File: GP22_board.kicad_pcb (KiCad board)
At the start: 2 copper layers, 100 x 100 mm, 115 parts, among them CON1 5V power input, IC1 ATMEGA328P-A, P1 TTLOut1, P10 CONN_02X02, P11 CONN_02X02, P12 CONN_02X02, P13 TTLOut2, P14 TTLOut3, P15 CONN_01X03, P2 SineInput, P3 TTLInput, P4 USB_OTG, P5 ICSP, P6 StraightThroughInput, P7 CONN_02X02, P8 CONN_02X02, P9 CONN_02X02, SW1 ROTARY_SWITCH_ALPS_SRBM, SW2 ROTARY_SWITCH_ALPS_SRBM, SW3 ROTARY_SWITCH_ALPS_SRBM, U1 RS 252-210, U10 XC6206, U11 ISO7242, U12 FT232RL, U2 GP22, U3 LTC6957-4, U4 ISO3088, U5 IDT49FCT, U6 LD1117S33TR, U7 MC74VHC1GT04, U8 SN74LV8154, U9 SC74HC165N, X1 TSX-3225 X1E0000210013, Y1 4MHz, Y2 32.768 kHz

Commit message: Board nearly done
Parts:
- added D6: ESDA5V3SC6, TO_SOT_Packages_SMD:SOT-23-5_HandSoldering, F.Cu at (190.5, 47.2)
- added D7: ESDA5V3SC6, TO_SOT_Packages_SMD:SOT-23-5_HandSoldering, F.Cu at (173.3, 52.5)
- moved C17 285.0 mm to (193.6, 81.2)
- moved R34 253.7 mm to (192.2, 84.6), turned to 90 degrees
- moved R33 225.6 mm to (187.8, 90.4), turned to 270 degrees
- moved C15 216.9 mm to (191.6, 100.4), turned to 270 degrees
- moved C16 195.2 mm to (186.6, 93.8), turned to 180 degrees
- moved Y1 169.8 mm to (205.0, 96.2), turned to 180 degrees
- moved Y2 138.6 mm to (210.3, 84.5), turned to 180 degrees
- moved C22 137.6 mm to (200.6, 102.8), turned to 180 degrees
- moved R36 133.2 mm to (200.6, 100.4), turned to 180 degrees
- moved C21 131.8 mm to (211.6, 96.4), turned to 270 degrees
- moved C23 130.7 mm to (214.0, 96.6), turned to 90 degrees
- moved R35 129.3 mm to (209.2, 96.4), turned to 270 degrees
- moved R37 120.6 mm to (212.2, 100.2), turned to 180 degrees
- moved U10 120.6 mm to (206.6, 101.0), turned to 180 degrees
- moved U8 93.7 mm to (231.0, 76.4)
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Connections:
- D1 pad 1: /InputCoupling/OutputS- -> (no net)
- D1 pad 3: /InputCoupling2/OutputS+ -> /InputCoupling/InputSignal
- D1 pad 4: /StraightThrough -> /InputCoupling/InputGnd
- D1 pad 5: /InputCoupling/OutputS+ -> (no net)
- SW1 pad 1b: /StraightThrough -> /TTLBuffered
- SW1 pad 2b: /SineRectified -> /StraightThrough
- SW1 pad 4a: /TTLBuffered -> /SineRectified
- SW2 pad 1b: /StraightThrough -> /TTLBuffered
- SW2 pad 2b: /SineRectified -> /StraightThrough
- SW2 pad 4a: /TTLBuffered -> /SineRectified
- SW3 pad 1b: /StraightThrough -> /TTLBuffered
- SW3 pad 2b: /SineRectified -> /StraightThrough
- SW3 pad 4a: /TTLBuffered -> /SineRectified
- U5 pad 2: /TTLBufferedOut2 -> /TTLBufferedOut3
- U5 pad 3: /TTLBufferedOut1 -> /TTLBufferedOut2
- U5 pad 4: /TTLBufferedOut3 -> /TTLBufferedOut1
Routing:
- net /TTLBufferedOut1: track 0.00 -> 84.7 mm
- net /TTLBufferedOut3: track 0.00 -> 83.8 mm
- net /TTLBufferedOut2: track 0.00 -> 81.8 mm
- net Net-(U8-Pad15): track 0.00 -> 38.0 mm
- net Net-(U8-Pad14): track 0.00 -> 36.7 mm
- net Net-(U8-Pad13): track 0.00 -> 35.5 mm
- net Net-(U8-Pad12): track 0.00 -> 34.2 mm
- net /GP22_VIO: track 0.00 -> 29.8 mm
- net /StraightThrough: track 168.1 -> 139.2 mm
- net /InputCoupling2/OutputS+: track 32.2 -> 60.4 mm
- net /InputCoupling2/InputSignal: track 9.79 -> 34.7 mm
- net /InputCoupling2/InputGnd: track 10.9 -> 35.1 mm
- net /SineRectified: track 103.0 -> 84.8 mm
- net /GP22_START: track 62.2 -> 46.5 mm
- net /TTLBufferedOut_toCounter: track 0.00 -> 12.9 mm
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- added copper zone on In2.Cu, net +3V3
- added copper zone on In2.Cu, net /GP22_VCC
- added copper zone on In1.Cu, net GND
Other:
- copper layers 2 -> 4

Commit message: DRC passes
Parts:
- removed C20: 100n, Capacitors_SMD:C_0805_HandSoldering
- removed R24, R25, R30, R31: 10k, Resistors_SMD:R_0805_HandSoldering
- added C26: 100n, Capacitors_SMD:C_0805_HandSoldering, F.Cu at (202.3, 89.5)
- added C27: 100n, Capacitors_SMD:C_0805_HandSoldering, F.Cu at (213.2, 87.1)
- added P16: FILT_SEL, Pin_Headers:Pin_Header_Straight_2x02_Pitch2.54mm, F.Cu at (217.2, 60.0)
- P15: value CONN_01X03 -> PWR_SEL
- moved C2 203.3 mm to (200.7, 99.9), turned to 180 degrees
- moved C1 197.4 mm to (201.4, 92.5)
- moved R2 194.4 mm to (199.1, 108.8), turned to 180 degrees
- moved R5 190.6 mm to (195.1, 99.1), turned to 270 degrees
- moved R9 183.3 mm to (210.3, 62.0)
- moved R6 179.0 mm to (210.0, 81.2)
- moved C3 174.1 mm to (210.0, 79.3), turned to 180 degrees
- moved R1 173.8 mm to (201.8, 84.4)
- moved R7 171.2 mm to (210.3, 60.0), turned to 180 degrees
- moved C5 164.2 mm to (206.3, 81.8), turned to 90 degrees
- moved R4 163.8 mm to (201.8, 82.5)
- moved CON1 160.2 mm to (220.8, 48.0), turned to 180 degrees
- moved C18 156.6 mm to (239.7, 59.6)
- moved U6 156.3 mm to (232.9, 62.8), turned to 180 degrees
- moved C19 138.1 mm to (240.7, 65.7)
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- renumbered C2 to C1, C1 to C2
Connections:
- net Net-(C12-Pad2) renamed /G1
- net Net-(C13-Pad2) renamed /G2
- net Net-(C14-Pad2) renamed /G3
- C1 pad 2: Net-(C2-Pad2) -> Net-(C1-Pad2)
- C2 pad 2: Net-(C1-Pad2) -> Net-(C2-Pad2)
- CON1 pad 1: Net-(C18-Pad1) -> Net-(CON1-Pad1)
- IC1 pad 11: /~CTR_CLR -> /REG_DATA
- IC1 pad 12: /CTR_LOAD -> /CTR_BIT_SEL
- IC1 pad 13: /CTR_BIT_SEL -> /CTR_LOAD
- IC1 pad 23: /LTC_FILTB -> /GP22_INT
- IC1 pad 24: /LTC_FILTA -> /GP22_EN_START
- IC1 pad 25: /GP22_INT -> /GP22_EN_STOP1
- IC1 pad 26: /GP22_EN_START -> /GP22_EN_STOP2
- IC1 pad 27: /GP22_EN_STOP1 -> /~CTR_CLR
- IC1 pad 28: /GP22_EN_STOP2 -> /REG_CLK
- IC1 pad 30: /REG_DATA -> /DIYino/D0/RX
- IC1 pad 31: /REG_LOAD -> /DIYino/D1/TX
- IC1 pad 32: /REG_CLK -> /REG_LOAD
- P15 pad 1: /Backplane_3V3 -> /Backplane_5V
- P15 pad 2: +3V3 -> Net-(C18-Pad1)
- P15 pad 3: Net-(P15-Pad3) -> Net-(CON1-Pad1)
- R7 pad 1: /LTC_FILTB -> Net-(P16-Pad2)
- R9 pad 2: /LTC_FILTA -> Net-(P16-Pad4)
- R_Ser1 pad 1: /REG_DATA -> /DIYino/D0/RX
- R_Ser2 pad 2: /REG_LOAD -> /DIYino/D1/TX
- U1 pad A13: /BPSubsheet/+5V -> /Backplane_5V
- U1 pad A15: /Backplane_3V3 -> /BPSubsheet/+3.3V
- U1 pad B13: /BPSubsheet/+5V -> /Backplane_5V
- U1 pad B15: /Backplane_3V3 -> /BPSubsheet/+3.3V
- U1 pad C13: /BPSubsheet/+5V -> /Backplane_5V
- U1 pad C15: /Backplane_3V3 -> /BPSubsheet/+3.3V
- U3 pad 1: /LTC_FILTA -> Net-(P16-Pad4)
- U3 pad 6: /LTC_FILTB -> Net-(P16-Pad2)
- U6 pad 2: Net-(P15-Pad3) -> +3V3
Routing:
- net GND: track 32.7 -> 129.9 mm, vias 25 -> 59
- net /CTR_BIT_SEL: track 0.00 -> 71.7 mm, vias 0 -> 1
- net /REG_CLK: track 0.00 -> 64.0 mm, vias 0 -> 1
- net /GP22_EN_STOP2: track 0.00 -> 61.5 mm, vias 0 -> 2
- net /REG_DATA: track 4.69 -> 63.8 mm, vias 0 -> 1
- net /REG_LOAD: track 4.85 -> 63.8 mm, vias 0 -> 1
- net /GP22_EN_STOP1: track 0.00 -> 57.3 mm, vias 0 -> 2
- net /~CTR_CLR: track 0.00 -> 50.4 mm, vias 0 -> 1
- net /CTR_LOAD: track 0.00 -> 45.7 mm, vias 0 -> 1
- net /GP22_CS: track 0.00 -> 41.7 mm, vias 0 -> 2
- net /Backplane_5V: track 0.00 -> 41.2 mm
- net /GP22_EN_START: track 0.00 -> 39.1 mm, vias 0 -> 3
- net /GP22_INT: track 0.00 -> 38.1 mm, vias 0 -> 2
- net /GP22_SCK: track 31.5 -> 66.6 mm, vias 0 -> 2
- net /GP22_MISO: track 9.59 -> 42.6 mm, vias 0 -> 1
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- removed copper zone on B.Cu, net GND

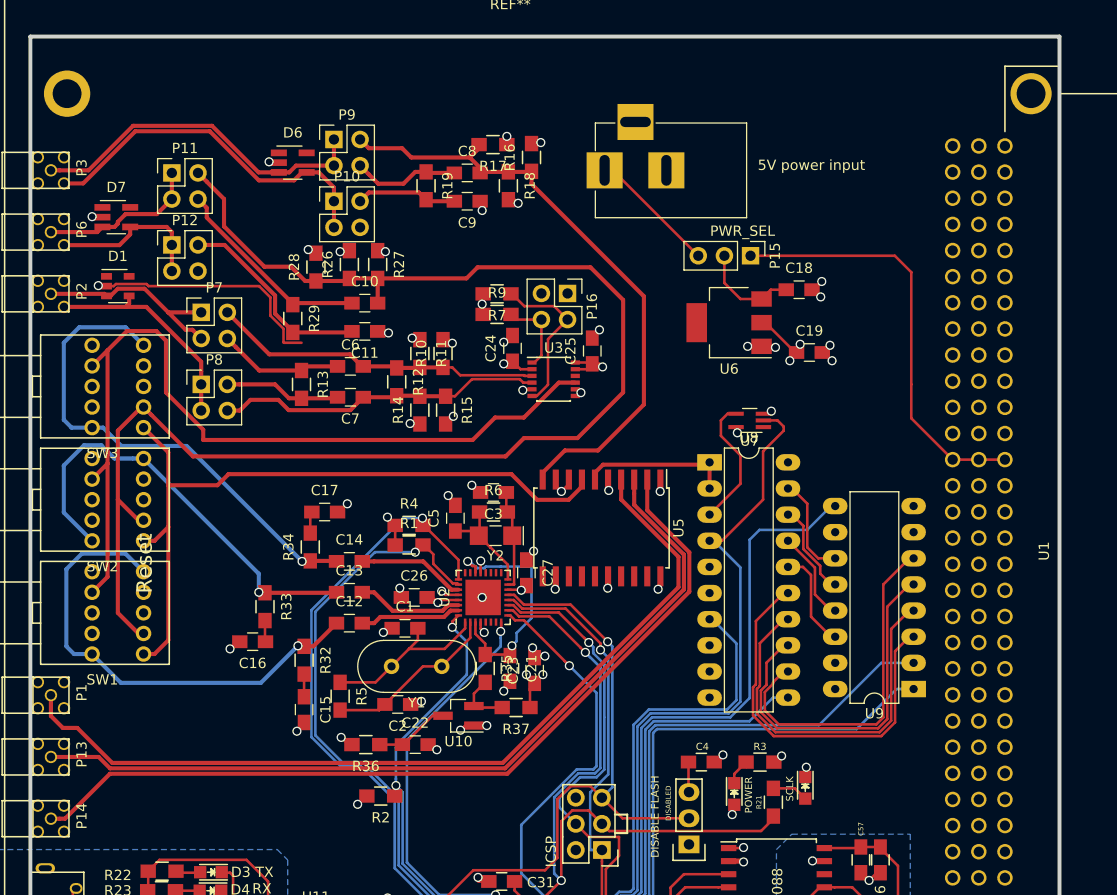
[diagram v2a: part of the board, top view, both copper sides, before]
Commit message: Silkscreen labelling
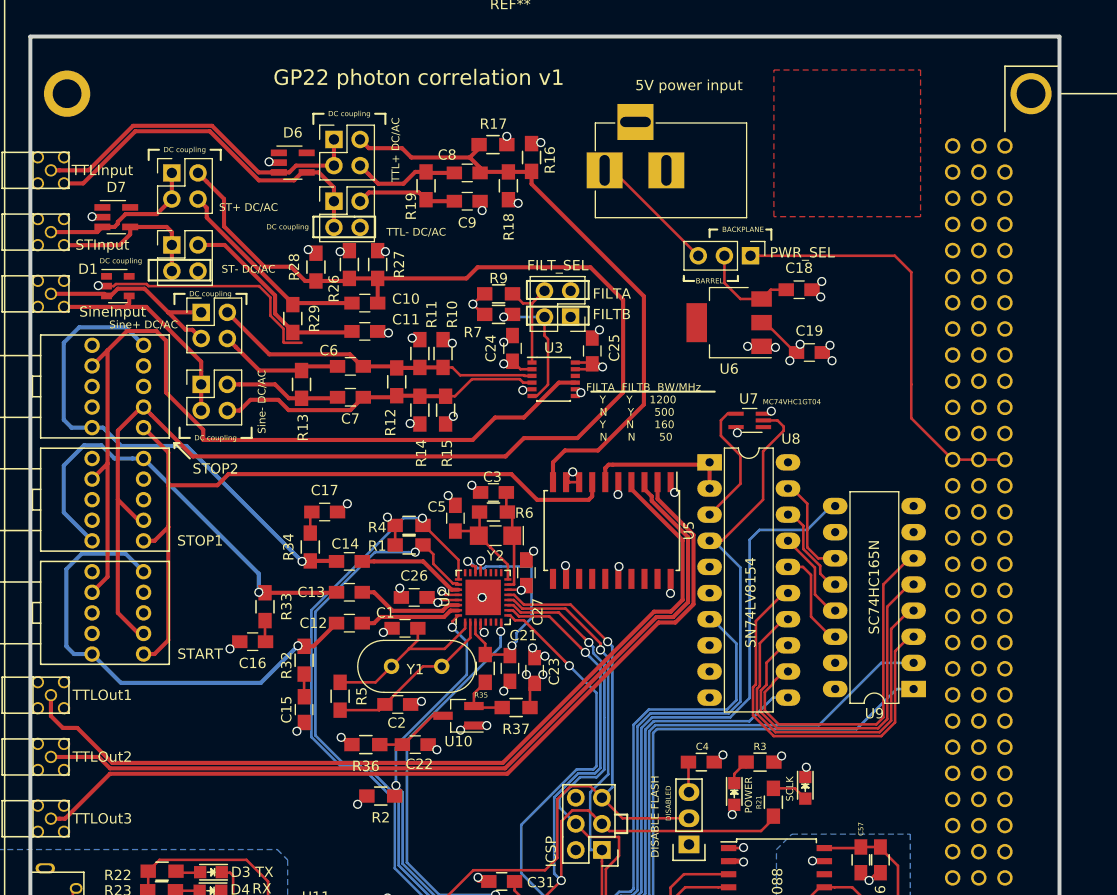
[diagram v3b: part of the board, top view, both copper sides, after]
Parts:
- added G***: LOGO, Custom:NPL_logo_mask, F.Cu at (244.2, 45.2)
- P10: value CONN_02X02 -> TTL- DC/AC
- P11: value CONN_02X02 -> ST+ DC/AC
- P12: value CONN_02X02 -> ST- DC/AC
- P6: value StraightThroughInput -> STInput
- P7: value CONN_02X02 -> Sine+ DC/AC
- P8: value CONN_02X02 -> Sine- DC/AC
- P9: value CONN_02X02 -> TTL+ DC/AC
- SW1: value ROTARY_SWITCH_ALPS_SRBM -> START
- SW2: value ROTARY_SWITCH_ALPS_SRBM -> STOP1
- SW3: value ROTARY_SWITCH_ALPS_SRBM -> STOP2
- moved P16 2.31 mm to (217.5, 62.2), turned to 180 degrees
- moved R7 2.01 mm to (210.5, 62.0)
- moved R9 2.01 mm to (210.5, 60.0)
- moved U5 1.03 mm to (221.5, 83.0)
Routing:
- net Net-(P16-Pad4): track 7.86 -> 9.98 mm
- net Net-(P16-Pad2): track 15.9 -> 13.9 mm, vias 0 -> 1
- net /TTLBuffered: track 70.5 -> 71.8 mm
- net +3V3: track 48.6 -> 49.8 mm
- net /TTLBufferedOut_toCounter: track 15.4 -> 14.3 mm
- net GND: track 129.9 -> 131.0 mm
- net /TTLBufferedOut3: track 83.8 -> 84.4 mm
- net /TTLBufferedOut2: track 81.8 -> 82.5 mm
- net /TTLBufferedOut1: track 84.7 -> 85.4 mm
- added copper zone on F.Cu, net (none)
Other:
- board text added: "BACKPLANE"
- board text added: "BARREL"
- board text added: "DC coupling"
- board text added: "FILTA"
- board text added: "FILTA FILTB BW/MHz Y Y 1200 N Y 500 Y N 160 N N 50"
- board text added: "FILTB"
- board text added: "GP22 photon correlation v1"
- board text removed: "Reset"

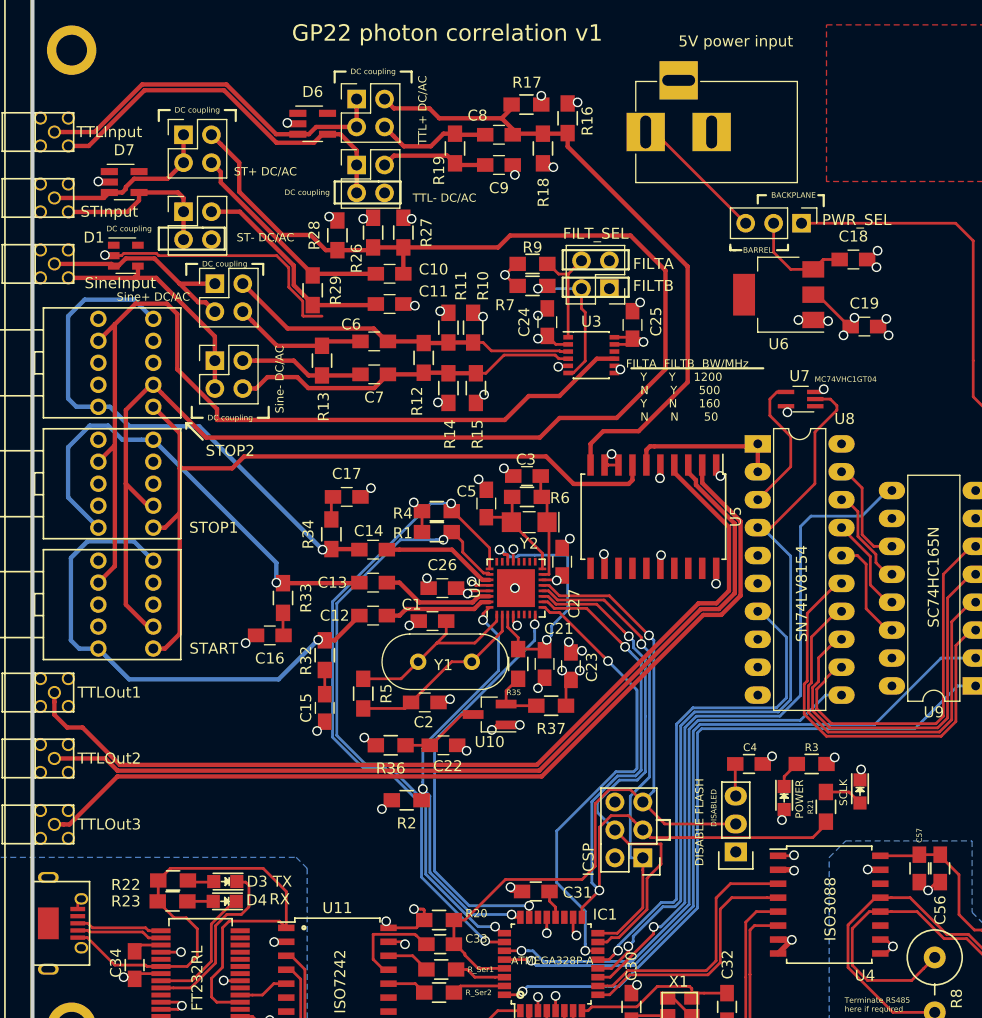
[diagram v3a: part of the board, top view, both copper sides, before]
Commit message: Tweaks to RF path
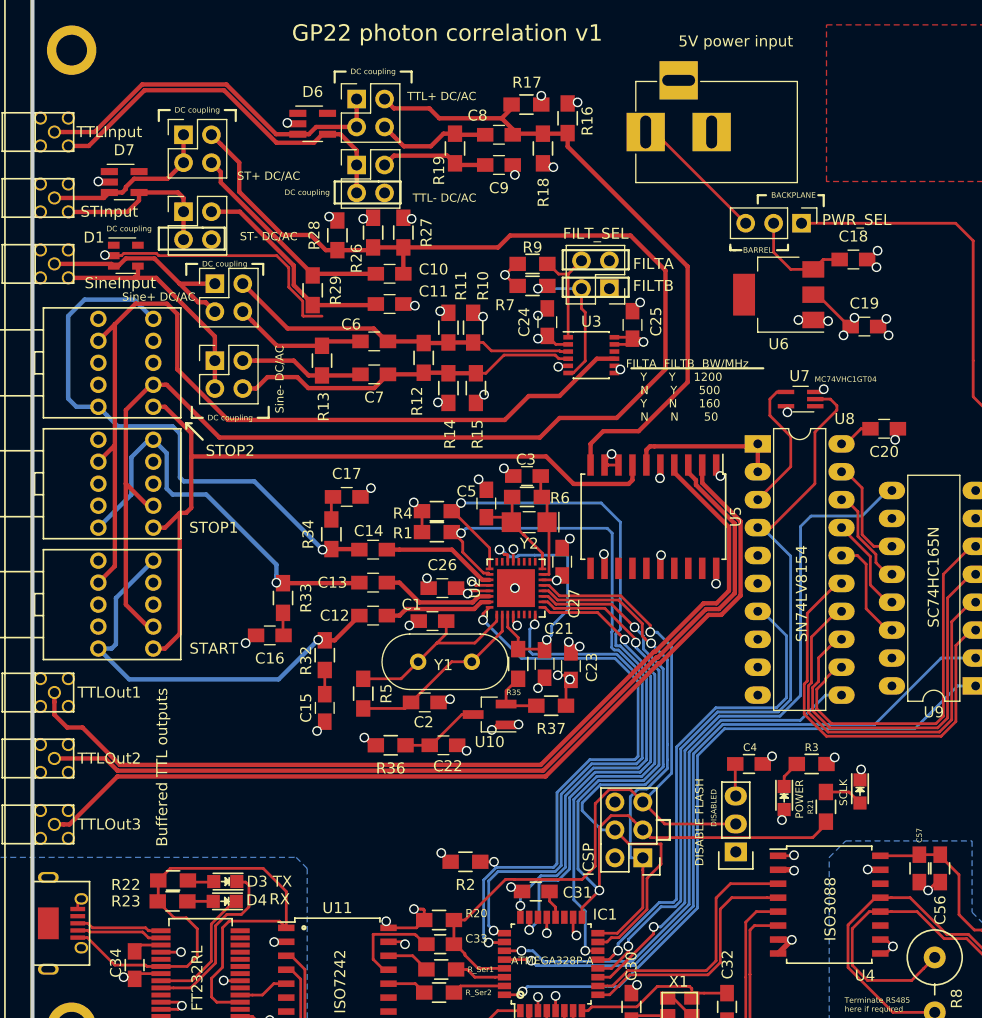
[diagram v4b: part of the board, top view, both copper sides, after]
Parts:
- added C20: 100n, Capacitors_SMD:C_0805_HandSoldering, F.Cu at (242.5, 75.0)
- P10: value TTL- DC/AC -> S- DC/AC
- P11: value ST+ DC/AC -> S+ DC/AC
- P12: value ST- DC/AC -> S- DC/AC
- P7: value Sine+ DC/AC -> S+ DC/AC
- P8: value Sine- DC/AC -> S- DC/AC
- P9: value TTL+ DC/AC -> S+ DC/AC
- moved R2 7.74 mm to (204.4, 114.4)
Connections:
- IC1 pad 23: /GP22_INT -> /GP22_EN_STOP2
- IC1 pad 24: /GP22_EN_START -> /GP22_EN_STOP1
- IC1 pad 25: /GP22_EN_STOP1 -> /GP22_INT
- IC1 pad 26: /GP22_EN_STOP2 -> /GP22_EN_START
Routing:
- net /GP22_EN_START: track 39.1 -> 56.3 mm
- net /GP22_INT: track 38.1 -> 50.5 mm
- net /GP22_EN_STOP2: track 61.5 -> 70.8 mm
- net /GP22_START: track 46.5 -> 38.1 mm
- net /GP22_EN_STOP1: track 57.3 -> 65.2 mm
- net /GP22_STOP1: track 42.8 -> 37.3 mm
- net /GP22_MOSI: track 47.9 -> 53.4 mm
- net /GP22_SCK: track 66.6 -> 71.4 mm
- net /GP22_CS: track 41.7 -> 45.2 mm
- net +3V3: track 49.8 -> 53.0 mm
- net /GP22_MISO: track 42.6 -> 45.3 mm
- net /GP22_STOP2: track 48.8 -> 51.2 mm
- net /ARD_RST: track 70.4 -> 72.7 mm
- net /REG_CLK: track 64.0 -> 62.8 mm
- net /REG_DATA: track 63.8 -> 62.6 mm
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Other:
- board text added: "Buffered TTL outputs"
- board text added: "ST+ DC/AC"
- board text added: "ST- DC/AC"
- board text added: "Sine+ DC/AC"
- board text added: "Sine- DC/AC"
- board text added: "TTL+ DC/AC"
- board text added: "TTL- DC/AC"
